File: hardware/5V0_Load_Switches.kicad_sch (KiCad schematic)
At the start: 28 parts, among them Q18 SI2302DDS-T1-GE3, Q19 SI2302DDS-T1-GE3, Q20 SI2302DDS-T1-GE3, U1 LMV321RIYLT, U10 INA199C3DCKR, U4 INA199C1DCKR, U5 NVTFS5116PLTAG, U6 NVTFS5116PLTAG, U7 NVTFS5116PLTAG, U9 INA199C3DCKR

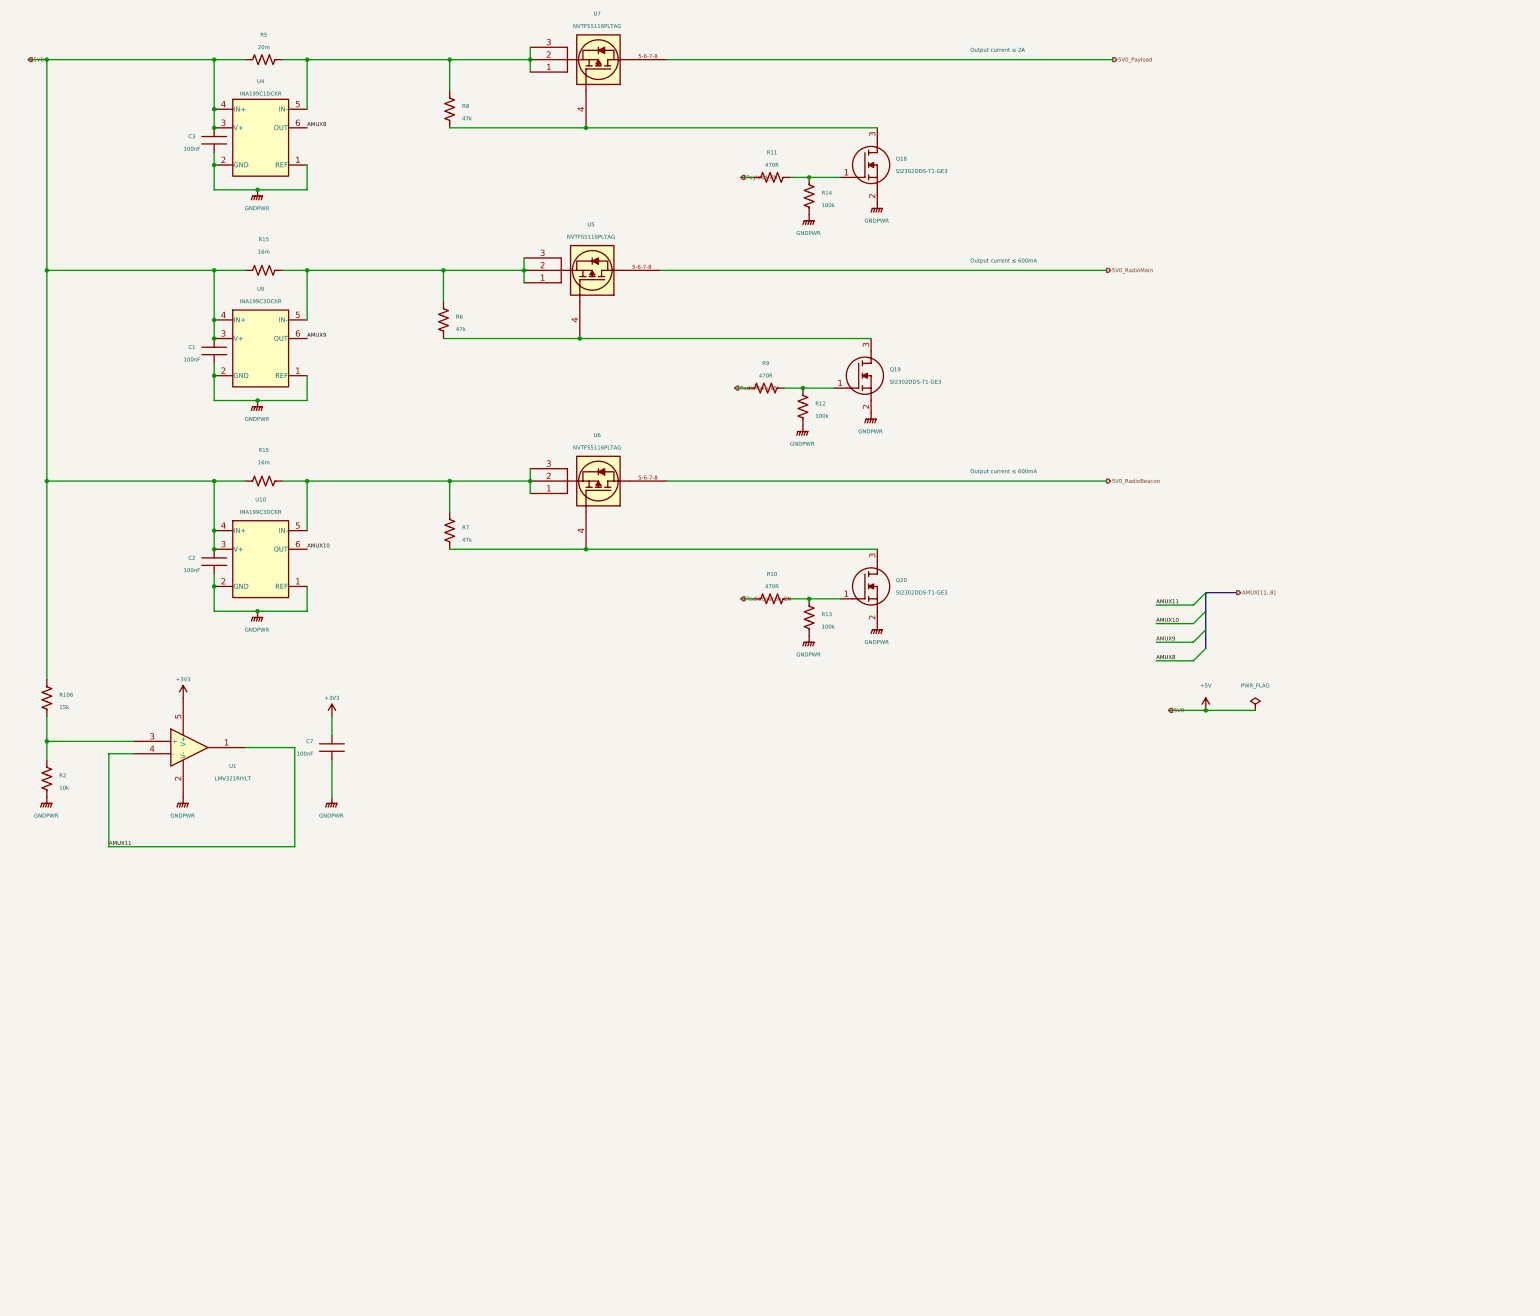
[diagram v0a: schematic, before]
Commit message: hardware: Improving the readability of schematics
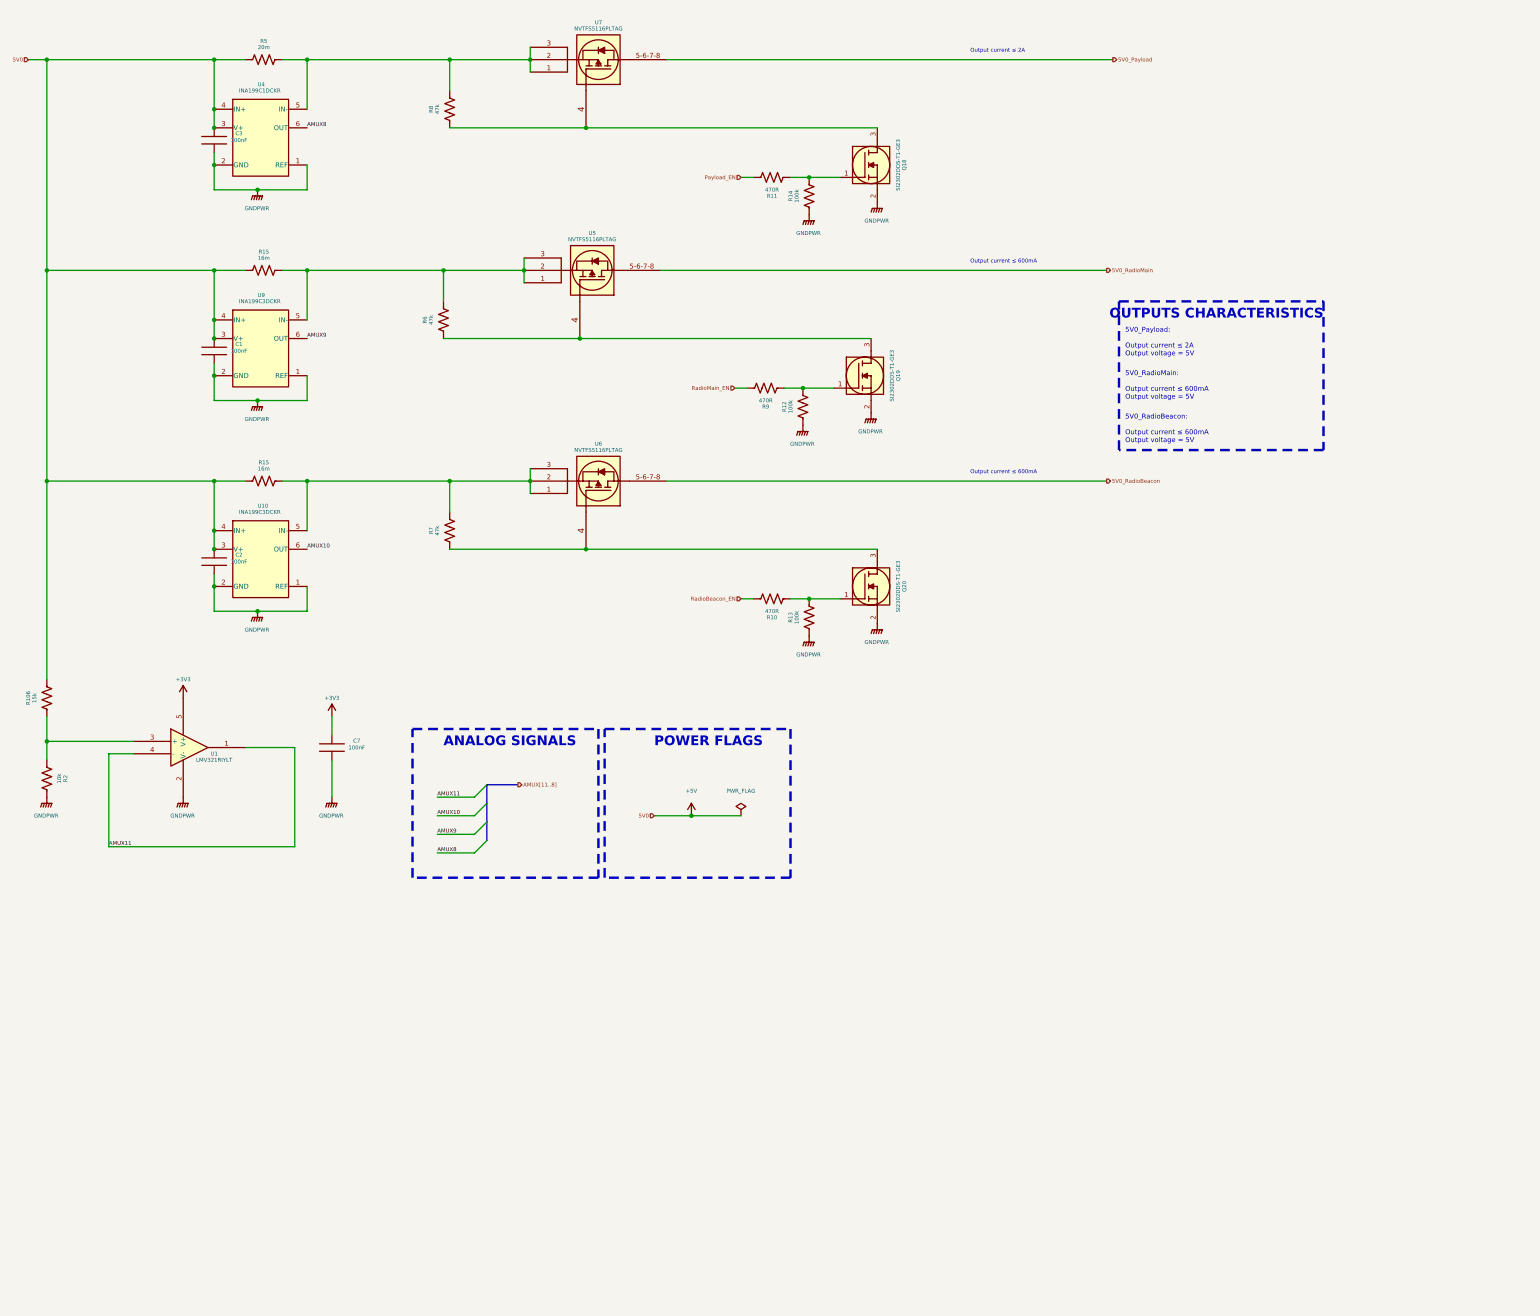
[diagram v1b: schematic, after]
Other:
- note added: "5V0_Payload: Output current ≤ 2A Output voltage = 5V"
- note added: "5V0_RadioBeacon: Output current ≤ 600mA Output voltage = 5V"
- note added: "5V0_RadioMain: Output current ≤ 600mA Output voltage = 5V"
- note added: "ANALOG SIGNALS"
- note added: "OUTPUTS CHARACTERISTICS"
- note added: "POWER FLAGS"

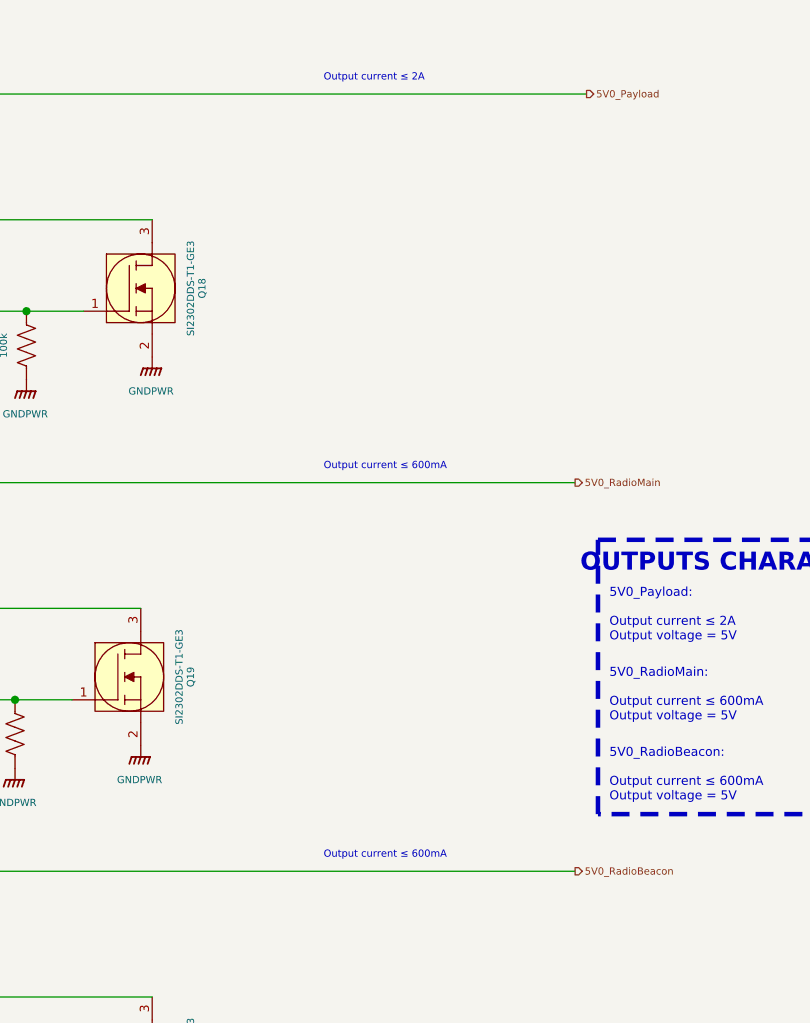
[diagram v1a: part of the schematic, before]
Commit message: hardware: Increasing the readability of the schematic and adding a table with the revision history
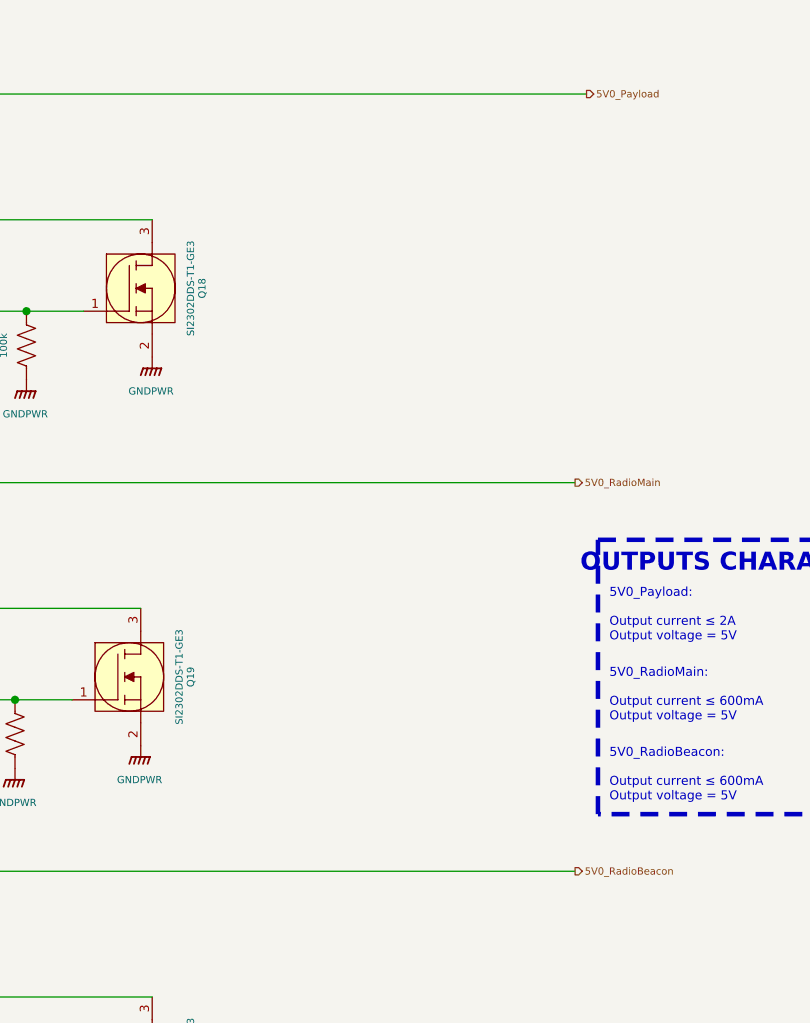
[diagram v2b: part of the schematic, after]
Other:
- note removed: "Output current ≤ 2A"
- note removed: "Output current ≤ 600mA"
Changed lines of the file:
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@@
     (effects (font (size 1 1) (color 0 0 0 1)) (justify left bottom))
-  )
-  (text "Output current ≤ 600mA" (at 212.09 71.12 0)
-    (effects (font (size 0.8 0.8)) (justify left bottom))
   )
   (text "ANALOG SIGNALS" (at 104.14 170.18 0)
@@
     (effects (font (size 1 1) (color 0 0 0 1)) (justify left bottom))
   )
-  (text "Output current ≤ 600mA" (at 212.09 114.3 0)
-    (effects (font (size 0.8 0.8)) (justify left bottom))
-  )
   (text "5V0_RadioBeacon:\n\nOutput current ≤ 600mA\nOutput voltage = 5V\n"
     (at 243.84 107.95 0)
     (effects (font (size 1 1) (color 0 0 0 1)) (justify left bottom))
   )
-  (text "Output current ≤ 2A" (at 212.09 27.94 0)
-    (effects (font (size 0.8 0.8)) (justify left bottom))
-  )
   (label "AMUX8" (at 102.87 191.77 0) (fields_autoplaced)

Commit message: hardware: Making improvements for first release
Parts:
- C1, C2, C3, C7: MPN (none) -> C0603C104K5RACTU; Manufacturer (none) -> KEMET; Package (none) -> SMD 0603; automotive Yes -> (none); automotive grade Grade 1 -> (none); capacitance 0.10 μF -> (none); category Cap -> (none); device class L1 Passive Components -> (none); device class L2 Capacitors -> (none); device class L3 Ceramic Capacitors -> (none); digikey description CAP CER 0.1UF 50V X7R 0603 -> (none); digikey part number 399-5089-2-ND -> (none); height 0.87mm -> (none); lead free Yes -> (none); library id 73022d3323b2b2b8 -> (none); manufacturer KEMET -> (none); material Ceramic -> (none); mouser part number 80-C0603C104K5R7867 -> (none); package 0603 -> (none); rohs Yes -> (none); temperature characteristic X7R -> (none); temperature coefficient 30ppm/°C -> (none); temperature range high +125°C -> (none); temperature range low -55°C -> (none); tolerance 0.1 -> (none); voltage rating 50 V -> (none)
- Q18, Q19, Q20: Height 1.12 -> (none); MPN (none) -> SI2302DDS-T1-GE3; Manufacturer (none) -> Vishay; Manufacturer_Name Vishay -> (none); Manufacturer_Part_Number SI2302DDS-T1-GE3 -> (none); Mouser Part Number 78-SI2302DDS-T1-GE3 -> (none); Mouser Price/Stock https://www.mouser.co.uk/ProductDetail/Vishay-Semiconductor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 -> (none); Package (none) -> SOT-23-3
- R10, R11, R9: MPN (none) -> CRCW0603470RFKEAHP; Manufacturer (none) -> Vishay; Package (none) -> SMD 0603; automotive Yes -> (none); automotive grade Grade 0 -> (none); category Res -> (none); composition Thick Film -> (none); device class L1 Passive Components -> (none); device class L2 Resistors -> (none); device class L3 Chip SMD Resistors -> (none); height 0.55mm -> (none); ipc land pattern name RESC16085X45 -> (none); lead free Yes -> (none); library id 3843bba7e74bf2ed -> (none); manufacturer Vishay -> (none); package 0603 -> (none); power 250mW -> (none); power rating 0.33W -> (none); resistance 470Ω -> (none); rohs Yes -> (none); series CRCW-HP e3 -> (none); temperature coefficient 100ppm/°C -> (none); temperature range high +155°C -> (none); temperature range low -55°C -> (none); tolerance 1% -> (none); voltage rating 75V -> (none)
- R12, R13, R14: Arrow Part Number CRCW0603100KFKEAHP -> (none); Arrow Price/Stock https://www.arrow.com/en/products/crcw0603100kfkeahp/vishay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 -> (none); Height 0.55 -> (none); MPN (none) -> CRCW0603100KFKEAHP; Manufacturer (none) -> Vishay; Manufacturer_Name Vishay -> (none); Manufacturer_Part_Number CRCW0603100KFKEAHP -> (none); Mouser Part Number 71-CRCW0603100KFKEAH -> (none); Mouser Price/Stock https://www.mouser.co.uk/ProductDetail/Vishay-Dale/CRCW0603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 -> (none); Package (none) -> SMD 0603
- R15: MPN (none) -> WSL2010R0330FEA; Manufacturer (none) -> Vishay; Package (none) -> SMD 2010
- R5: Arrow Part Number WSL2010R0200FEA -> (none); Arrow Price/Stock https://www.arrow.com/en/products/wsl2010r0200fea/vishay -> (none); MPN (none) -> WSL2010R0200FEA; Manufacturer (none) -> Vishay; Manufacturer_Name Vishay -> (none); Manufacturer_Part_Number WSL2010R0200FEA -> (none); Mouser Part Number 71-WSL2010R0200FEA -> (none); Mouser Price/Stock https://www.mouser.co.uk/ProductDetail/Vishay-Dale/WSL2010R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 -> (none); Package (none) -> SMD 2010
- R6, R7, R8: MPN (none) -> CRCW060347K0FKEAHP; Manufacturer (none) -> Vishay; Package (none) -> SMD 0603; automotive Yes -> (none); automotive grade Grade 0 -> (none); category Res -> (none); composition Thick Film -> (none); device class L1 Passive Components -> (none); device class L2 Resistors -> (none); device class L3 Chip SMD Resistors -> (none); height 0.55mm -> (none); ipc land pattern name RESC16085X45 -> (none); lead free Yes -> (none); library id 41c6336701360bfc -> (none); manufacturer Vishay -> (none); package 0603 -> (none); power 250mW -> (none); power rating 0.33W -> (none); resistance 47kΩ -> (none); rohs Yes -> (none); series CRCW-HP e3 -> (none); temperature coefficient 100ppm/°C -> (none); temperature range high +155°C -> (none); temperature range low -55°C -> (none); tolerance 1% -> (none); voltage rating 75V -> (none)
- U1: MPN (none) -> LMV321RIYLT; Manufacturer (none) -> STMicroelectronics; Package (none) -> SOT-23-5
- U10, U9: footprint Package_TO_SOT_SMD:SOT-363_SC-70-6 -> footprints:INA199C3DCKR; symbol INA199C3DCKR:INA199xxDCK -> INA199C3DCKR:INA199C3DCKR; MPN (none) -> INA199C3DCKR; Manufacturer (none) -> TI; Package (none) -> SC70-6
- U4: symbol INA199C1DCKR:INA199xxDCK -> INA199C1DCKR:INA199C1DCKR; MPN (none) -> INA199C1DCKR; Manufacturer (none) -> TI; Package (none) -> SC70-6
- U5, U6, U7: MPN (none) -> NVTFS5116PLTAG; Manufacturer (none) -> onsemi; Package (none) -> WDFN-8
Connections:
- net AMUX10: no longer U10.6 (OUT)
- net AMUX8: no longer U4.6 (OUT)
- net AMUX9: no longer U9.6 (OUT)
- net GNDPWR: no longer U10.1 (REF), U4.1 (REF), U9.1 (REF)
- net at R15.2, R7.2, U6.1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: no longer U10.5 (IN-)
- net at R15.2, R6.2, U5.1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: no longer U9.5 (IN-)
- net at R5.2, R8.2, U7.1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: no longer U4.5 (IN-)
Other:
- moved on the sheet: U10, U4, U9
